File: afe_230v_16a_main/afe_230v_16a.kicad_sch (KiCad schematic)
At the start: 75 parts, among them J4 MCV 1,5/ 6-G-3,81, J5 HBUS16, J6 pinheader_1x6, P1 06-14-03_rectifier, U1 ${SIM.PARAMS}, U17 1_element_2_current, U2 AD8538, U20 watt_hour_meter_bidirectional, U21 3w_ne, U3 AD8538_dnp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

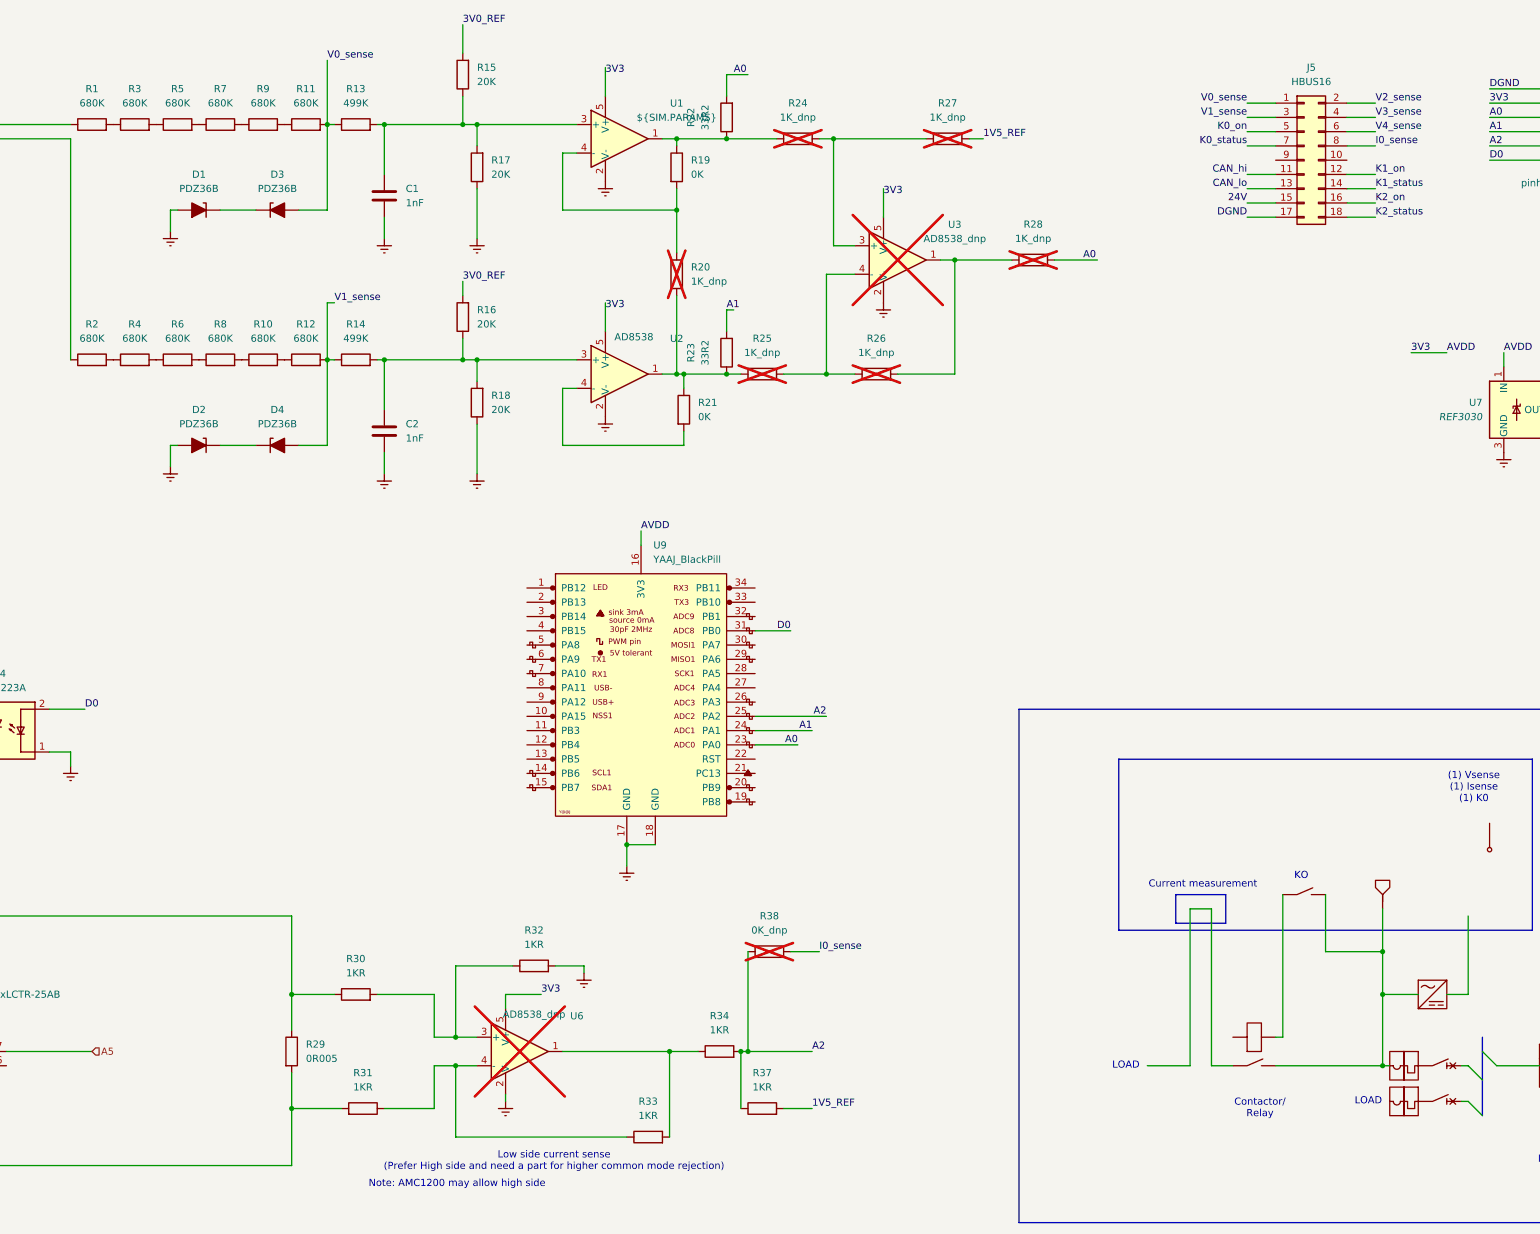
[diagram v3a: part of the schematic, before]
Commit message: adjusted HBUS, DNP, & fixed A5toA2
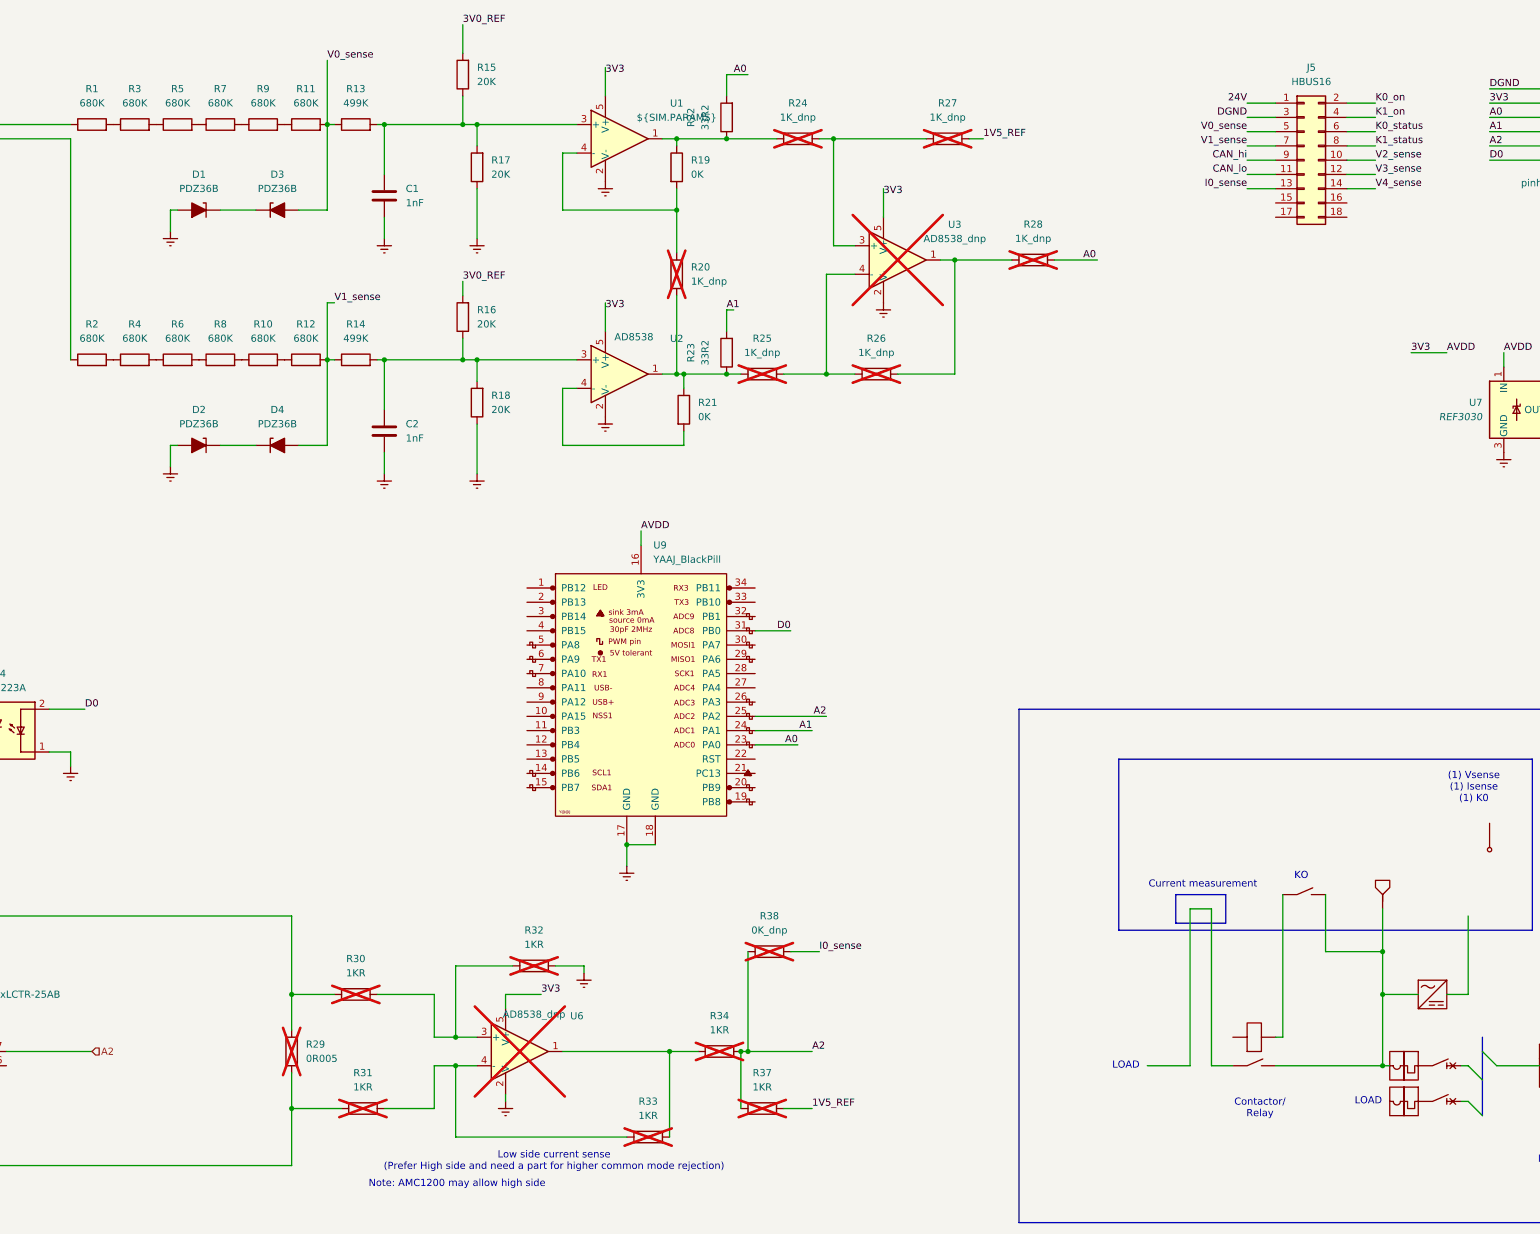
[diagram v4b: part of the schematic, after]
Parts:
- R29, R30, R31, R32, R33, R34, R37: now not fitted
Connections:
- net A5 is gone; now on net A2: U5.7 (VIOUT)
- net 24V: now also J5.1 (Pin_1); no longer J5.15 (Pin_15)
- net CAN_hi: now also J5.9 (Pin_9); no longer J5.11 (Pin_11)
- net CAN_lo: now also J5.11 (Pin_11); no longer J5.13 (Pin_13)
- net DGND: now also J5.3 (Pin_3); no longer J5.17 (Pin_17)
- net I0_sense: now also J5.13 (Pin_13); no longer J5.8 (Pin_8)
- net K0_on: now also J5.2 (Pin_2); no longer J5.5 (Pin_5)
- net K0_status: now also J5.6 (Pin_6); no longer J5.7 (Pin_7)
- net K1_on: now also J5.4 (Pin_4); no longer J5.12 (Pin_12)
- net K1_status: now also J5.8 (Pin_8); no longer J5.14 (Pin_14)
- net V0_sense: now also J5.5 (Pin_5); no longer J5.1 (Pin_1)
- net V1_sense: now also J5.7 (Pin_7); no longer J5.3 (Pin_3)
- net V2_sense: now also J5.10 (Pin_10); no longer J5.2 (Pin_2)
- net V3_sense: now also J5.12 (Pin_12); no longer J5.4 (Pin_4)
- net V4_sense: now also J5.14 (Pin_14); no longer J5.6 (Pin_6)
- net at U20.: now also T16.
- net at T16.: now also T17.; no longer U20.
- net at C8.: now also T10.
- net at T10.: now also T8.; no longer C8.
- net at C7.: now also C3., P1., T8., U8.
- net at T17.: now also C12.; no longer T16.
- net at T7.: now also C3.
- net at T11.: now also C9.; no longer T9.
- net at C9.: no longer T11.
- net at U21.: no longer C12.
- net K2_on: no longer names the net of J5.16 (Pin_16)
- net K2_status: no longer names the net of J5.18 (Pin_18)
- new net: T11., T9.
- new net: C12., U21.
- now unconnected: P1., U8.
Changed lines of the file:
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@@
 	(wire
 		(pts
-			(xy 300.99 49.53) (xy 306.07 49.53)
-		)
-		(stroke
-			(width 0)
-			(type default)
-		)
-	)
-	(wire
-		(pts
 			(xy 53.34 196.85) (xy 53.34 193.04)
 		)
@@
 	(wire
 		(pts
+			(xy 318.77 39.37) (xy 323.85 39.37)
+		)
+		(stroke
+			(width 0)
+			(type default)
+		)
+	)
+	(wire
+		(pts
 			(xy 314.96 180.34) (xy 325.12 180.34)
 		)
@@
 	(wire
 		(pts
-			(xy 300.99 46.99) (xy 306.07 46.99)
+			(xy 300.99 29.21) (xy 306.07 29.21)
 		)
 		(stroke
@@
 	(wire
 		(pts
-			(xy 318.77 49.53) (xy 323.85 49.53)
-		)
-		(stroke
-			(width 0)
-			(type default)
-		)
-	)
-	(wire
-		(pts
 			(xy 196.85 77.47) (xy 199.39 77.47)
 		)
@@
 	(wire
 		(pts
+			(xy 300.99 39.37) (xy 306.07 39.37)
+		)
+		(stroke
+			(width 0)
+			(type default)
+		)
+	)
+	(wire
+		(pts
 			(xy 181.61 80.01) (xy 179.07 80.01)
 		)
@@
 	(wire
 		(pts
-			(xy 300.99 29.21) (xy 306.07 29.21)
-		)
-		(stroke
-			(width 0)
-			(type default)
-		)
-	)
-	(wire
-		(pts
 			(xy 118.11 90.17) (xy 124.46 90.17)
 		)
@@
 	(wire
 		(pts
-			(xy 318.77 46.99) (xy 323.85 46.99)
-		)
-		(stroke
-			(width 0)
-			(type default)
-		)
-	)
-	(wire
-		(pts
 			(xy 344.17 39.37) (xy 359.41 39.37)
 		)
@@
 	)
 	(label "K0_status"
-		(at 300.99 36.83 180)
+		(at 323.85 34.29 0)
 		(effects
 			(font
 				(size 1.27 1.27)
 			)
-			(justify right bottom)
+			(justify left bottom)
 		)
 	)
@@
 	)
 	(label "V1_sense"
-		(at 300.99 31.75 180)
+		(at 300.99 36.83 180)
 		(effects
 			(font
@@
 	)
 	(label "V3_sense"
-		(at 323.85 31.75 0)
+		(at 323.85 41.91 0)
 		(effects
 			(font
@@
 		)
 	)
-	(label "K2_status"
-		(at 323.85 49.53 0)
-		(effects
-			(font
-				(size 1.27 1.27)
-			)
-			(justify left bottom)
-		)
-	)
 	(label "CAN_hi"
-		(at 300.99 41.91 180)
+		(at 300.99 39.37 180)
 		(effects
 			(font
@@
 	)
 	(label "V2_sense"
-		(at 323.85 29.21 0)
+		(at 323.85 39.37 0)
 		(effects
 			(font
@@
 	)
 	(label "I0_sense"
-		(at 323.85 36.83 0)
+		(at 300.99 44.45 180)
 		(effects
 			(font
 				(size 1.27 1.27)
 			)
-			(justify left bottom)
+			(justify right bottom)
 		)
 	)
@@
 	)
 	(label "V4_sense"
-		(at 323.85 34.29 0)
+		(at 323.85 44.45 0)
 		(effects
 			(font
@@
 	)
 	(label "K0_on"
-		(at 300.99 34.29 180)
+		(at 323.85 29.21 0)
 		(effects
 			(font
 				(size 1.27 1.27)
 			)
-			(justify right bottom)
+			(justify left bottom)
 		)
 	)
@@
 	)
 	(label "K1_on"
-		(at 323.85 41.91 0)
+		(at 323.85 31.75 0)
 		(effects
 			(font
@@
 	)
 	(label "CAN_lo"
-		(at 300.99 44.45 180)
+		(at 300.99 41.91 180)
 		(effects
 			(font
@@
 	)
 	(label "24V"
-		(at 300.99 46.99 180)
+		(at 300.99 29.21 180)
 		(effects
 			(font
@@
 		)
 	)
-	(label "K2_on"
-		(at 323.85 46.99 0)
-		(effects
-			(font
-				(size 1.27 1.27)
-			)
-			(justify left bottom)
-		)
-	)
 	(label "3V0_REF"
 		(at 161.29 60.96 0)
@@
 	)
 	(label "K1_status"
-		(at 323.85 44.45 0)
+		(at 323.85 36.83 0)
 		(effects
 			(font
@@
 	)
 	(label "DGND"
-		(at 300.99 49.53 180)
+		(at 300.99 31.75 180)
 		(effects
 			(font
@@
 	)
 	(label "V0_sense"
-		(at 300.99 29.21 180)
+		(at 300.99 34.29 180)
 		(effects
 			(font
@@
 		)
 	)
-	(hierarchical_label "A5"
+	(hierarchical_label "A2"
 		(shape input)
 		(at 95.25 198.12 0)
@@
 		(in_bom yes)
 		(on_board yes)
-		(dnp no)
+		(dnp yes)
 		(fields_autoplaced yes)
 		(property "Reference" "R33"
@@
 		(in_bom yes)
 		(on_board yes)
-		(dnp no)
+		(dnp yes)
 		(fields_autoplaced yes)
 		(property "Reference" "R32"
@@
 		(in_bom yes)
 		(on_board yes)
-		(dnp no)
+		(dnp yes)
 		(property "Reference" "R31"
 			(at 143.51 201.93 90)
@@
 		(in_bom yes)
 		(on_board yes)
-		(dnp no)
+		(dnp yes)
 		(fields_autoplaced yes)
 		(property "Reference" "R29"
@@
 		(in_bom yes)
 		(on_board yes)
-		(dnp no)
+		(dnp yes)
 		(property "Reference" "R37"
 			(at 214.63 201.93 90)
@@
 		(in_bom yes)
 		(on_board yes)
-		(dnp no)
+		(dnp yes)
 		(fields_autoplaced yes)
 		(property "Reference" "R34"
@@
 		(in_bom yes)
 		(on_board yes)
-		(dnp no)
+		(dnp yes)
 		(fields_autoplaced yes)
 		(property "Reference" "R30"

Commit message: located daughterboard & updated connector
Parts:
- added R39: 0, Resistor_SMD:R_0805_2012Metric, symbol Device:R
- J6: value pinheader_1x6 -> pinheader_2x6_socket; footprint Connector_PinHeader_2.54mm:PinHeader_1x06_P2.54mm_Vertical -> Connector_PinHeader_2.54mm:PinHeader_2x06_P2.54mm_Vertical; symbol Connector_Generic:Conn_01x06 -> Connector_Generic:Conn_02x06_Odd_Even
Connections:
- net 3V3: now also J6.4 (Pin_4); no longer J6.2 (Pin_2)
- net A0: now also J6.6 (Pin_6); no longer J6.3 (Pin_3)
- net A1: now also J6.8 (Pin_8); no longer J6.4 (Pin_4)
- net A2: now also J6.10 (Pin_10); no longer J6.5 (Pin_5)
- net D0: now also J6.12 (Pin_12); no longer J6.6 (Pin_6)
- net DGND: now also J6.2 (Pin_2), R39.2; no longer J6.1 (Pin_1)
- net Earth: now also J6.1 (Pin_1), R39.1
- net at U20.: now also T16.
- net at T16.: now also T17.; no longer U20.
- net at C8.: now also T10.
- net at T10.: now also T8.; no longer C8.
- net at C7.: now also C3., P1., T8., U8.
- net at T17.: now also C12.; no longer T16.
- net at T7.: now also C3.
- net at T11.: now also C9.; no longer T9.
- net at C9.: no longer T11.
- net at U21.: no longer C12.
- new net: T11., T9.
- new net: C12., U21.
- now unconnected: P1., U8.
